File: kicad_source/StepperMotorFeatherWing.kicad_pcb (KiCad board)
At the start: 2 copper layers, 100 x 60 mm, 118 parts, among them CN1 ADAFRUIT_FEATHER, CN10 691322310004, CN11 BM05B-SRSS-TB, CN2 DNI, CN20 691322310004, CN21 BM05B-SRSS-TB, CN3 BM04B-SRSS-TB, CN4 CONN_01X04, CN5 691322310002, CN6 691313710002, Q1 IPD90P03P4L- 04, U1 TMC5130A-TA, U2 TMC5130A-TA, U3 LM1085ISX-ADJ/NOPB, U4 LM75BD, U9 IFX91041EJV, Y1 ECS-3225MV-160-BN-TR

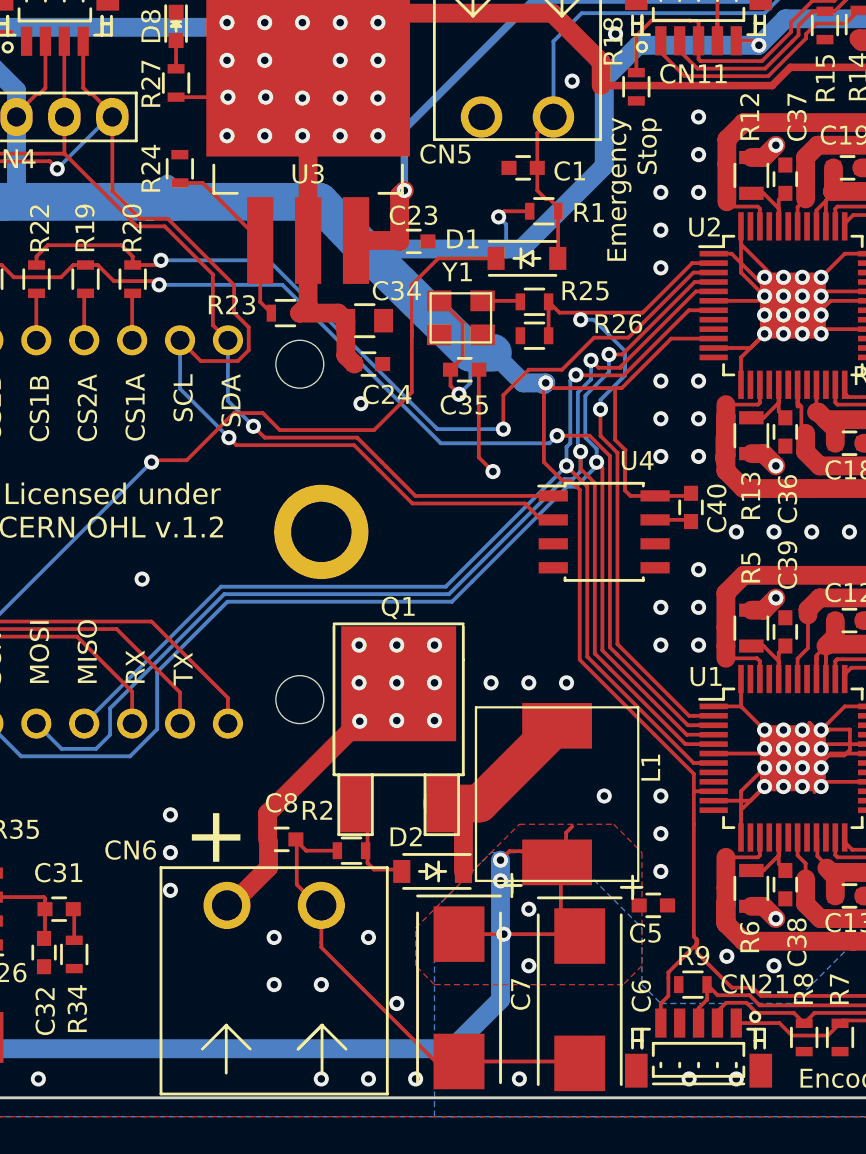
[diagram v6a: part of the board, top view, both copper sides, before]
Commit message: corrected position of mounting holes for heat spreader, added information on input voltage
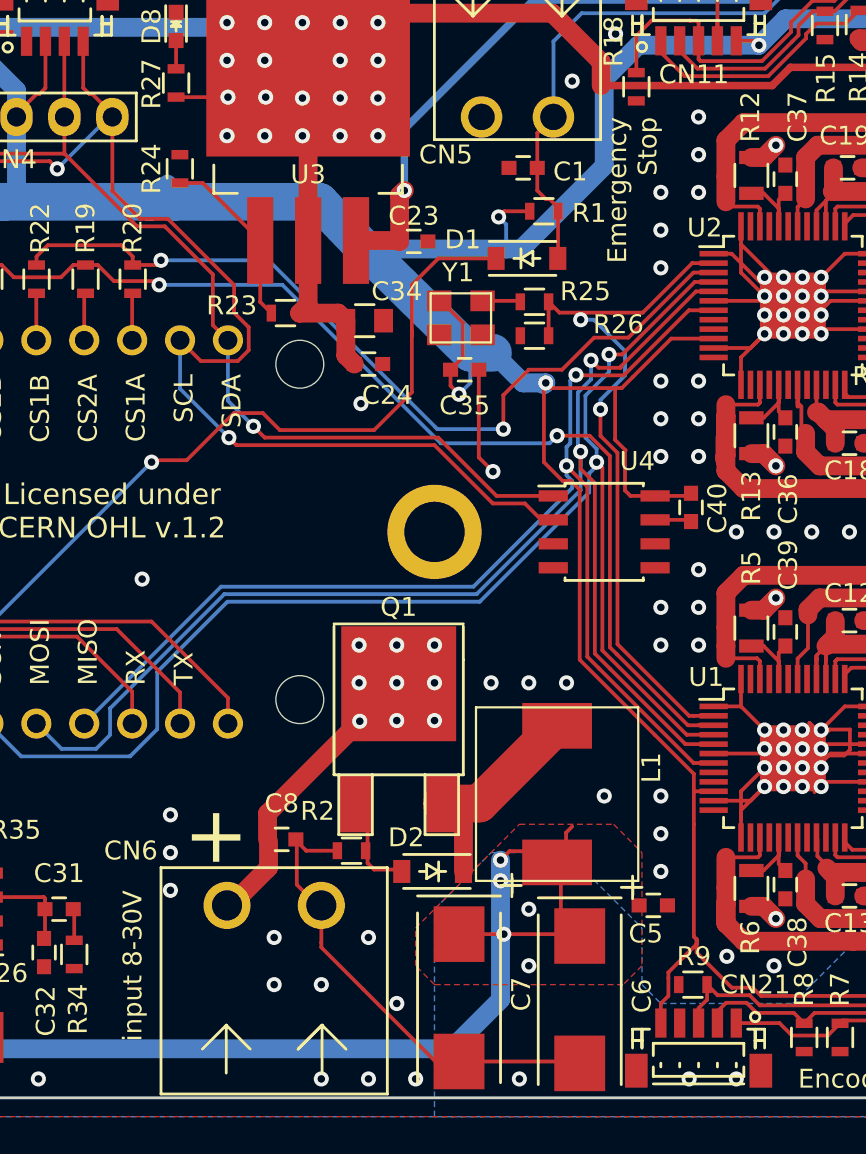
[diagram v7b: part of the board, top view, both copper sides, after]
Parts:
- moved MECH5 6.00 mm to (106.0, 96.0)
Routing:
- net MISO: track 64.6 -> 65.7 mm
- net MOSI: track 70.2 -> 70.8 mm
- net SCK: track 72.8 -> 73.4 mm
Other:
- board text added: "input 8-30V"

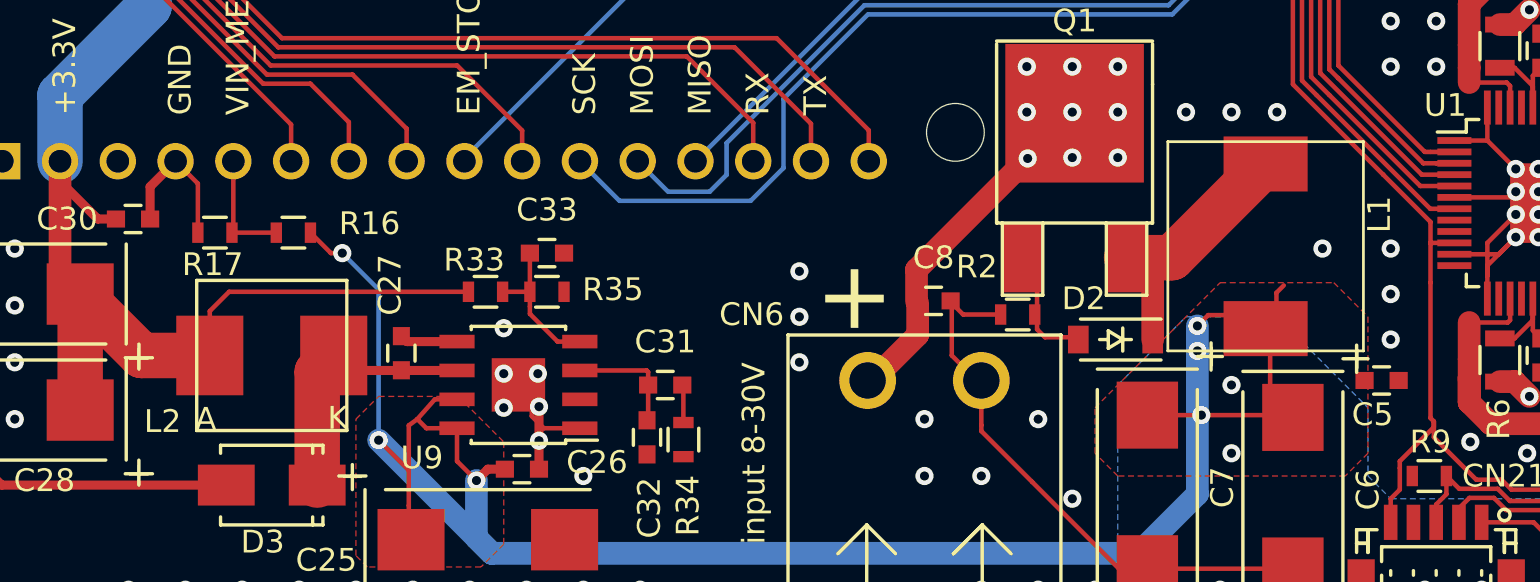
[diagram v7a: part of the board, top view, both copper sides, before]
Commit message: changed L1 and L2 to Sumida 0624CDMCCDS for better availability
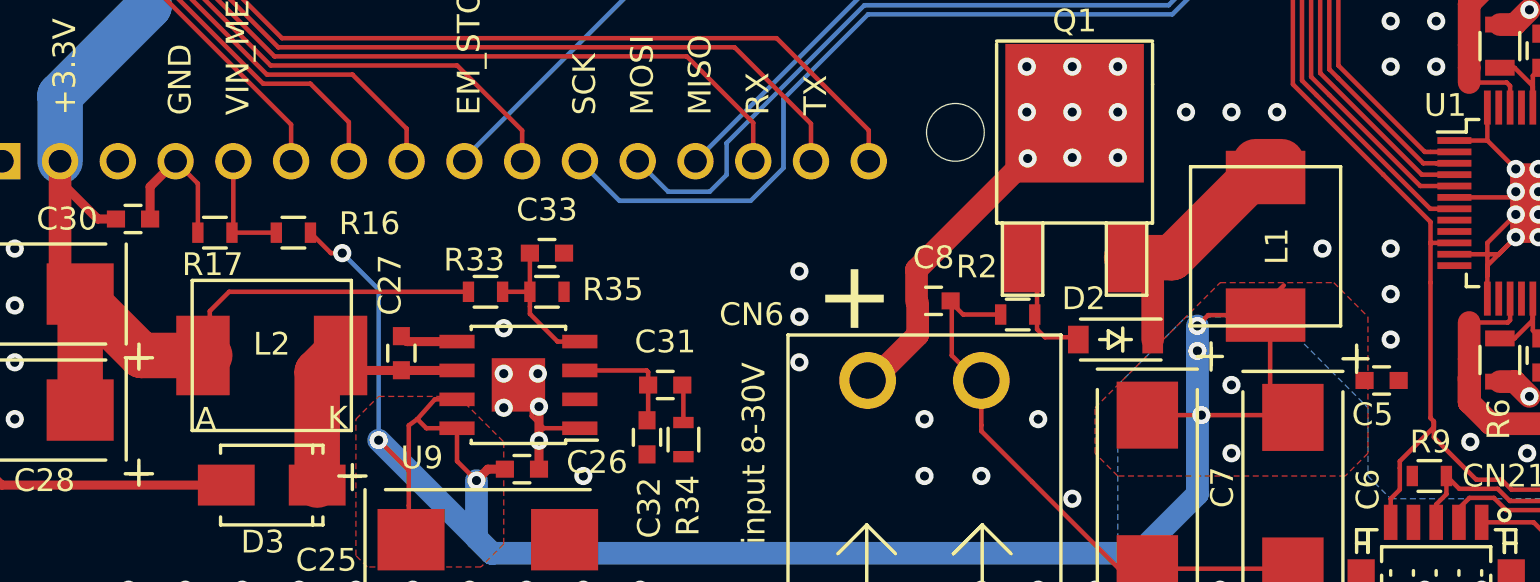
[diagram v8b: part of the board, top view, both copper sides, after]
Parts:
- L1: value 744373580022 -> 0624CDMCCDS-R22MC; footprint L_power:WE-LHMI80xx -> L_power:Sumida-0624CDMCCDS
- L2: value 74437346220 -> 0624CDMCCDS-220MC; footprint L_power:WE-LHMI70xx -> L_power:Sumida-0624CDMCCDS
